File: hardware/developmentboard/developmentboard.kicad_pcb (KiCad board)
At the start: 2 copper layers, 221.8 x 78 mm, 38 parts, among them J1 SPI Header, J2 Power Header, J3 Hall Effect Header, U1 ADS7960, U10 DRV5053, U11 DRV5053, U12 DRV5053, U13 DRV5053, U14 LM4040DBZ-2.5, U2 DRV5053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

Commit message: reworked things on develpoment
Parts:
- removed J2: Power Header, Connector_PinHeader_2.54mm:PinHeader_1x02_P2.54mm_Vertical
- removed REF** (x4): MountingHole_4.3mm_M4, MountingHole:MountingHole_4.3mm_M4
- added H1: MountingHole, MountingHole:MountingHole_4.3mm_M4, F.Cu at (255.9, 120.2)
- added H2: MountingHole, MountingHole:MountingHole_4.3mm_M4, F.Cu at (255.9, 52.2)
- added H3: MountingHole, MountingHole:MountingHole_4.3mm_M4, F.Cu at (44.4, 52.4)
- added H4: MountingHole, MountingHole:MountingHole_4.3mm_M4, F.Cu at (44.3, 120.1)
- J1: value SPI Header -> Conn_01x06_Male; footprint Connector_PinHeader_2.54mm:PinHeader_1x04_P2.54mm_Vertical -> Connector_PinHeader_2.54mm:PinHeader_1x06_P2.54mm_Vertical
- moved J1 0.32 mm to (258.5, 91.0)
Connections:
- J1 pad 1: RX -> TX
- J1 pad 2: TX -> CS
- J1 pad 3: CS -> SCLK
- J1 pad 4: SCLK -> RX
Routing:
- net TX: track 28.7 -> 18.7 mm
- net RX: track 20.6 -> 13.3 mm
- net SCLK: track 14.4 -> 19.8 mm
- net CS: vias 0 -> 1

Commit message: RP2040 Footprint Reset - See last commit
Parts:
- J1: value Conn_01x06_Male -> Brain Header
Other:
- board text added: "Brain Header"
- board text removed: "PWR"
- board text removed: "SPI"

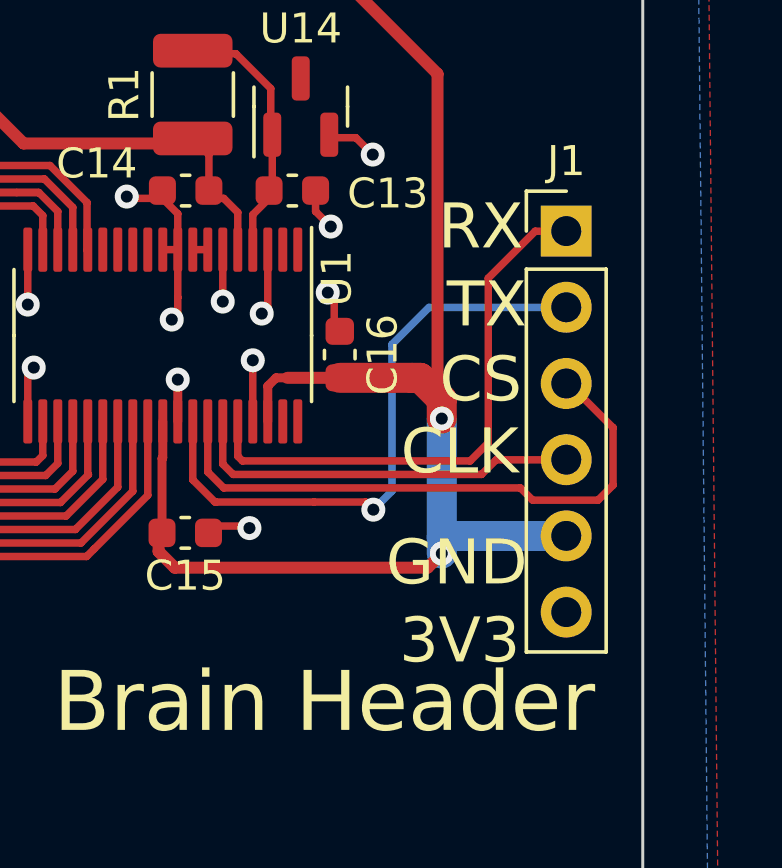
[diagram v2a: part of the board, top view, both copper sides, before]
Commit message: output file changes AND notes! Octave is now limited between 9 2 which corresponds to a piano range of C8 to C1, there are 3 notes below C1, that we will not be able to produce.
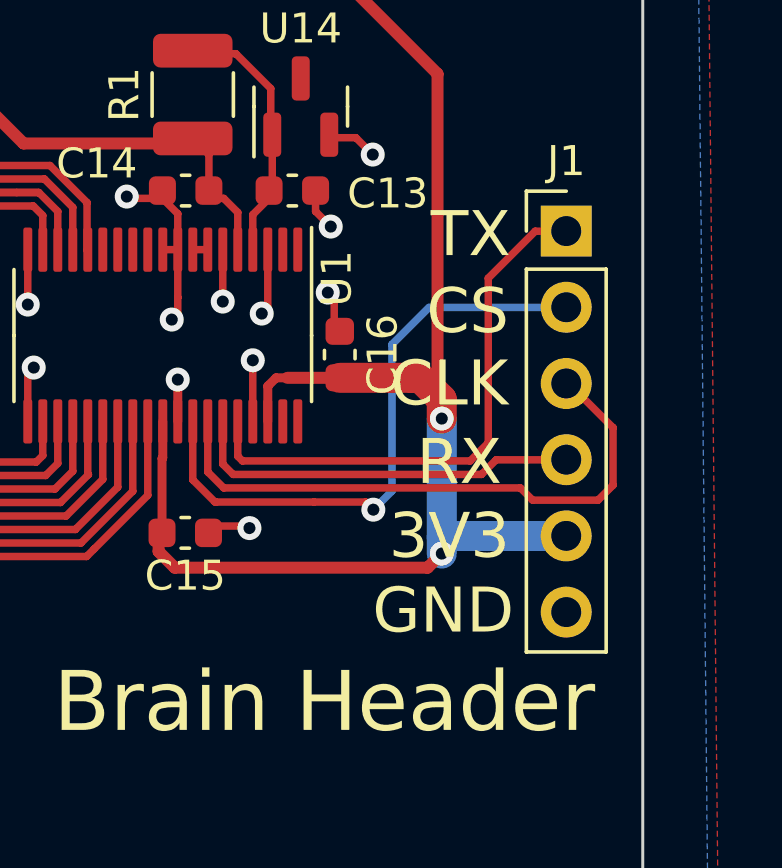
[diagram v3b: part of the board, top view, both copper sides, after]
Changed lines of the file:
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@@
     (effects (font (size 2 2) (thickness 0.3)))
   )
-  (gr_text "GND\n" (at 254.894 102.056) (layer "F.SilkS")
+  (gr_text "GND\n" (at 254.4438 103.6598) (layer "F.SilkS")
     (effects (font (size 1.5 1.5) (thickness 0.3)))
   )
@@
     (effects (font (size 1.5 1.5) (thickness 0.3)))
   )
-  (gr_text "CLK\n" (at 254.994 98.356) (layer "F.SilkS")
-    (effects (font (size 1.5 1.5) (thickness 0.3)))
-  )
-  (gr_text "TX\n" (at 255.894 93.456) (layer "F.SilkS")
+  (gr_text "CLK\n" (at 254.647 96.0906) (layer "F.SilkS")
+    (effects (font (size 1.5 1.5) (thickness 0.3)))
+  )
+  (gr_text "TX\n" (at 255.3582 91.1122) (layer "F.SilkS")
     (effects (font (size 1.5 1.5) (thickness 0.3)))
   )
@@
     (effects (font (size 1.5 1.5) (thickness 0.3)))
   )
-  (gr_text "3V3\n" (at 254.994 104.656) (layer "F.SilkS")
+  (gr_text "3V3\n" (at 254.647 101.1706) (layer "F.SilkS")
     (effects (font (size 1.5 1.5) (thickness 0.3)))
   )
@@
     (effects (font (size 2 2) (thickness 0.3)))
   )
-  (gr_text "CS\n" (at 255.694 95.956) (layer "F.SilkS")
+  (gr_text "CS\n" (at 255.2566 93.6776) (layer "F.SilkS")
     (effects (font (size 1.5 1.5) (thickness 0.3)))
   )
@@
     (effects (font (size 1.5 1.5) (thickness 0.3)))
   )
-  (gr_text "RX" (at 255.694 90.856) (layer "F.SilkS")
+  (gr_text "RX" (at 254.9772 98.7068) (layer "F.SilkS")
     (effects (font (size 1.5 1.5) (thickness 0.3)))
   )
@@
     (connect_pads (clearance 0))
     (min_thickness 0.254)
-    (keepout (tracks allowed) (vias allowed) (pads allowed ) (copperpour not_allowed) (footprints allowed))
+    (keepout (tracks allowed) (vias allowed) (pads allowed) (copperpour not_allowed) (footprints allowed))
     (fill (thermal_gap 0.508) (thermal_bridge_width 0.508))
     (polygon
